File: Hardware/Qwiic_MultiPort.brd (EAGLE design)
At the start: 25.4 x 25.4 mm, 25 parts, among them J1 QWIIC_RIGHT_ANGLE, J2 QWIIC_RIGHT_ANGLE, J3 QWIIC_RIGHT_ANGLE, J4 QWIIC_RIGHT_ANGLE

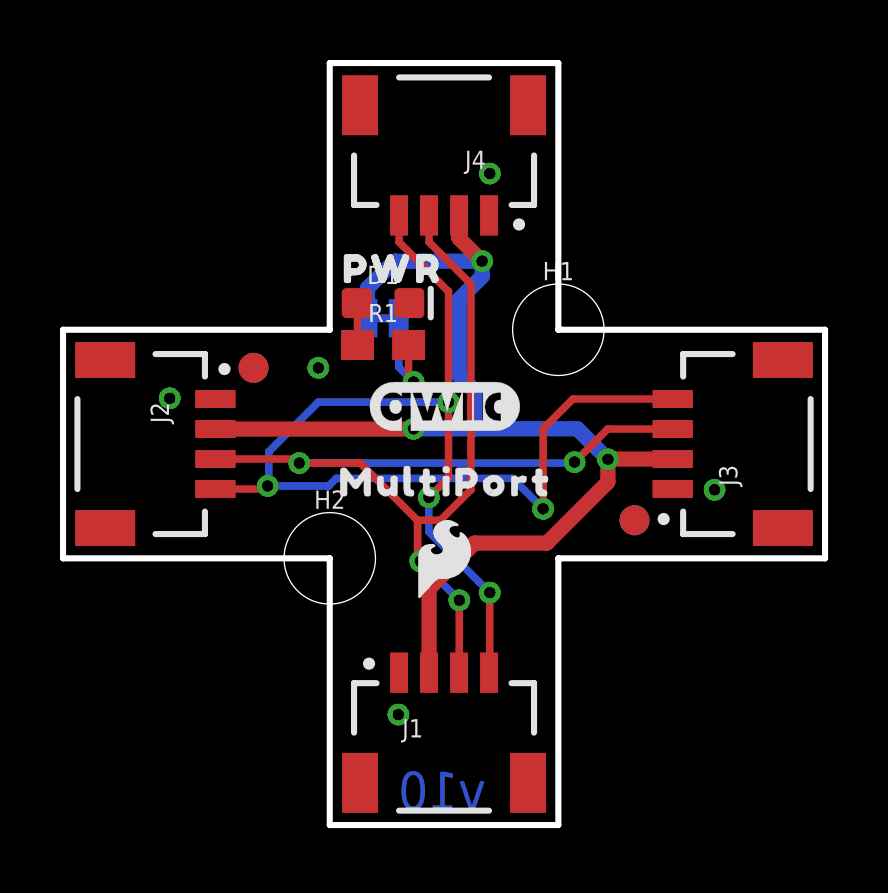
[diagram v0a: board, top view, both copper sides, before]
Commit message: MultiPort - Pete's notes
Reduced fiducial size to Micro
Moved PWR LED jumper and generated inverted label for jumper
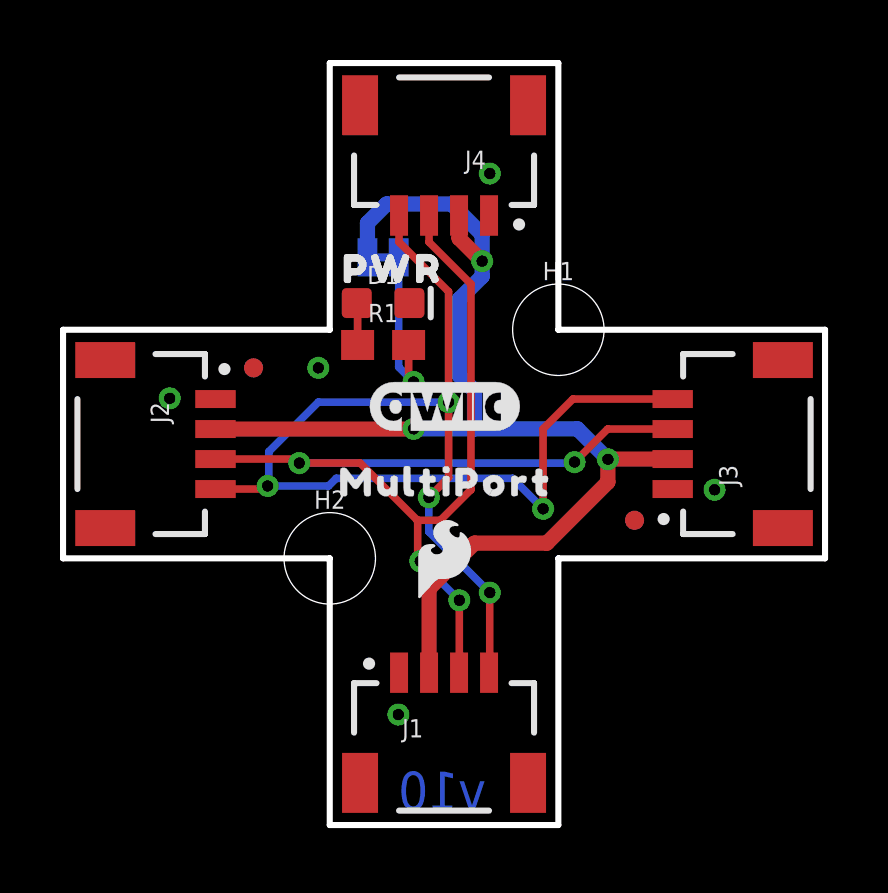
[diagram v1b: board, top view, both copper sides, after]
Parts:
- removed U$3: (no value), output:PWR0
- added U$5: (no value), output:#PWR#0
- FD1, FD2, FD3, FD4: value FIDUCIAL1X2 -> FIDUCIALUFIDUCIAL; device SparkFun-Aesthetics:FIDUCIAL-1X2 -> SparkFun-Aesthetics:FIDUCIAL-MICRO
- moved JP1 2.03 mm to (10.7, 18.9)
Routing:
- net N$2: track 3.63 -> 5.66 mm
- net 3.3V: track 39.8 -> 41.2 mm
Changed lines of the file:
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@@
 <element name="U$11" library="output" package="MULTI0" value="" x="15.24" y="4.191" smashed="yes" rot="MR0"/>
 <element name="U$13" library="output" package="PORT0" value="" x="14.986" y="2.794" smashed="yes" rot="MR0"/>
-<element name="FD1" library="SparkFun-Aesthetics" package="FIDUCIAL-1X2" value="FIDUCIAL1X2" x="6.35" y="15.24" smashed="yes" rot="MR0"/>
-<element name="FD2" library="SparkFun-Aesthetics" package="FIDUCIAL-1X2" value="FIDUCIAL1X2" x="6.35" y="15.24" smashed="yes"/>
-<element name="FD3" library="SparkFun-Aesthetics" package="FIDUCIAL-1X2" value="FIDUCIAL1X2" x="19.05" y="10.16" smashed="yes"/>
-<element name="FD4" library="SparkFun-Aesthetics" package="FIDUCIAL-1X2" value="FIDUCIAL1X2" x="19.05" y="10.16" smashed="yes" rot="MR0"/>
-<element name="JP1" library="SparkFun-Jumpers" package="SMT-JUMPER_2_NC_TRACE_SILK" package3d_urn="urn:adsk.eagle:package:39281/1" value="PWR_LED" x="10.668" y="16.891" smashed="yes" rot="MR0">
-<attribute name="NAME" x="10.668" y="18.034" size="0.6096" layer="26" font="vector" ratio="20" rot="MR0" align="bottom-center"/>
-<attribute name="VALUE" x="10.668" y="15.748" size="0.6096" layer="28" font="vector" ratio="20" rot="MR0" align="top-center"/>
+<element name="FD1" library="SparkFun-Aesthetics" package="FIDUCIAL-MICRO" value="FIDUCIALUFIDUCIAL" x="6.35" y="15.24" smashed="yes" rot="MR0"/>
+<element name="FD2" library="SparkFun-Aesthetics" package="FIDUCIAL-MICRO" value="FIDUCIALUFIDUCIAL" x="6.35" y="15.24" smashed="yes"/>
+<element name="FD3" library="SparkFun-Aesthetics" package="FIDUCIAL-MICRO" value="FIDUCIALUFIDUCIAL" x="19.05" y="10.16" smashed="yes"/>
+<element name="FD4" library="SparkFun-Aesthetics" package="FIDUCIAL-MICRO" value="FIDUCIALUFIDUCIAL" x="19.05" y="10.16" smashed="yes" rot="MR0"/>
+<element name="JP1" library="SparkFun-Jumpers" package="SMT-JUMPER_2_NC_TRACE_SILK" package3d_urn="urn:adsk.eagle:package:39281/1" value="PWR_LED" x="10.668" y="18.923" smashed="yes" rot="MR0">
+<attribute name="NAME" x="10.668" y="20.066" size="0.6096" layer="26" font="vector" ratio="20" rot="MR0" align="bottom-center"/>
+<attribute name="VALUE" x="10.668" y="17.78" size="0.6096" layer="28" font="vector" ratio="20" rot="MR0" align="top-center"/>
 </element>
 <element name="LOGO1" library="SparkFun-Aesthetics" package="QWIIC_5MM" value="QWIIC_LOGO_5MM" x="12.7" y="13.97" smashed="yes"/>
@@
 <element name="LOGO4" library="SparkFun-Aesthetics" package="SFE_LOGO_NAME_.2" value="SFE_LOGO_NAME.2_INCH" x="12.7" y="12.7" smashed="yes" rot="MR0"/>
 <element name="U$1" library="output" package="PWR0" value="" x="8.636" y="18.542" smashed="yes"/>
-<element name="U$3" library="output" package="PWR0" value="" x="12.954" y="18.542" smashed="yes" rot="MR0"/>
 <element name="U$4" library="output" package="MULTIPORT0" value="" x="8.509" y="11.43" smashed="yes"/>
+<element name="U$5" library="output" package="#PWR#0" value="" x="15.621" y="18.923" smashed="yes" rot="MR0"/>
 </elements>
 <signals>
@@
 <wire x1="13.962" y1="18.796" x2="13.97" y2="18.796" width="0.508" layer="1"/>
 <via x="13.97" y="18.796" extent="1-16" drill="0.381"/>
-<wire x1="13.97" y1="18.796" x2="11.049" y2="18.796" width="0.508" layer="16"/>
-<wire x1="11.049" y1="18.796" x2="10.1473" y2="17.8943" width="0.508" layer="16"/>
 <wire x1="13.97" y1="18.796" x2="13.97" y2="18.288" width="0.508" layer="16"/>
 <wire x1="13.97" y1="18.288" x2="13.208" y2="17.526" width="0.508" layer="16"/>
@@
 <wire x1="13.716" y1="14.478" x2="13.716" y2="13.208" width="0.508" layer="16"/>
 <wire x1="13.208" y1="17.526" x2="13.208" y2="14.986" width="0.508" layer="16"/>
-<wire x1="10.1473" y1="16.891" x2="10.1473" y2="17.8943" width="0.508" layer="16"/>
+<wire x1="13.97" y1="18.796" x2="13.97" y2="19.685" width="0.508" layer="16"/>
+<wire x1="13.97" y1="19.685" x2="12.954" y2="20.701" width="0.508" layer="16"/>
+<wire x1="12.954" y1="20.701" x2="10.7823" y2="20.701" width="0.508" layer="16"/>
+<wire x1="10.7823" y1="20.701" x2="10.1473" y2="20.066" width="0.508" layer="16"/>
+<wire x1="10.1473" y1="18.923" x2="10.1473" y2="20.066" width="0.508" layer="16"/>
 </signal>
 <signal name="N$1">
@@
 <via x="11.684" y="14.7701" extent="1-16" drill="0.381"/>
 <wire x1="11.684" y1="14.7701" x2="11.1887" y2="15.2654" width="0.254" layer="16"/>
-<wire x1="11.1887" y1="15.2654" x2="11.1887" y2="16.891" width="0.254" layer="16"/>
+<wire x1="11.1887" y1="15.2654" x2="11.1887" y2="18.923" width="0.254" layer="16"/>
 </signal>
 </signals>

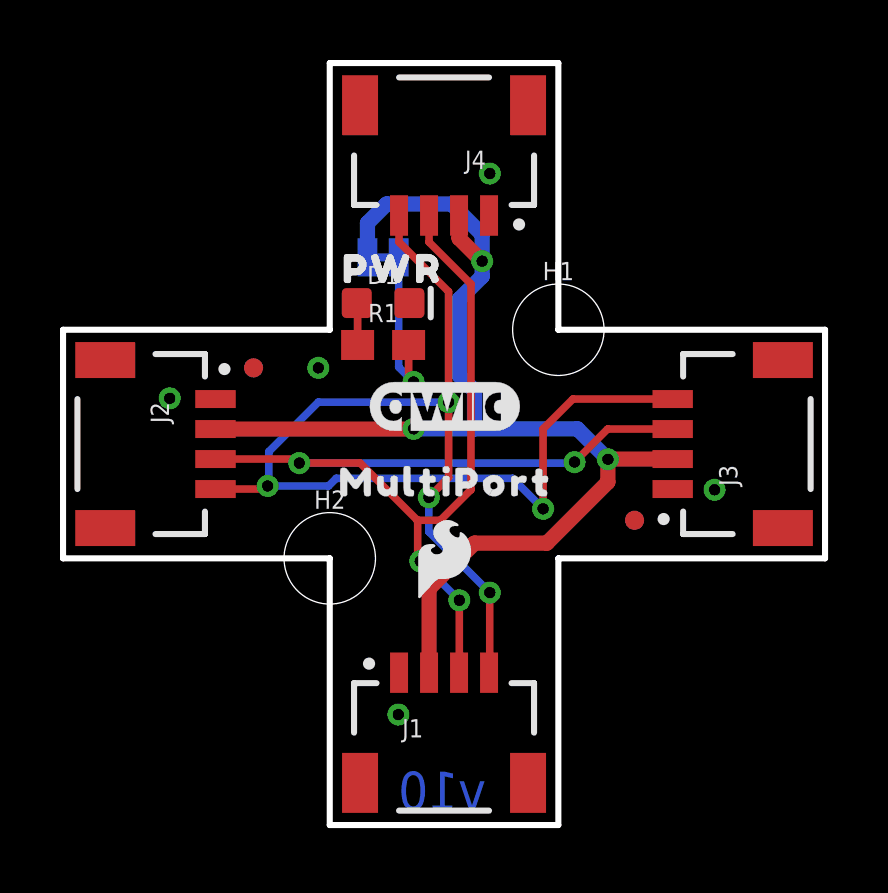
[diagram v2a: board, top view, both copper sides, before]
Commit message: re-route MultiPort in daisy chain configuration
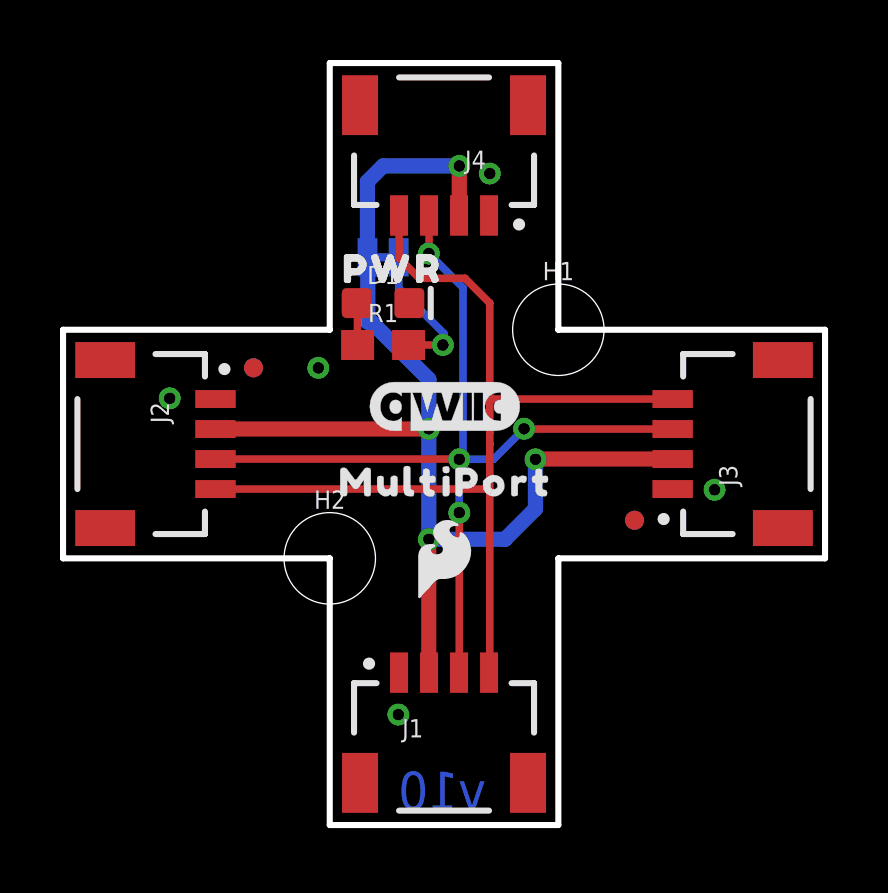
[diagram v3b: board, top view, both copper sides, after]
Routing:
- net SCL: track 43.8 -> 32.6 mm, vias 5 -> 0
- net SDA: track 38.1 -> 31.4 mm
- net 3.3V: track 41.2 -> 39.5 mm, vias 3 -> 4
- net N$2: track 5.66 -> 4.71 mm
